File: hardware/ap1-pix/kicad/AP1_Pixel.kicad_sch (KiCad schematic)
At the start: 40 parts, among them J1 ENTRADA 5-24V, J2 PIXELES 1, J3 PIXELES 2, J4 PIXELES 3, J5 PIXELES 4, J7 PROGRAMADOR, U1 INA238, U2 LMR16006XDDC, U3 74HCT125D, U4 M24C02-WMN6TP

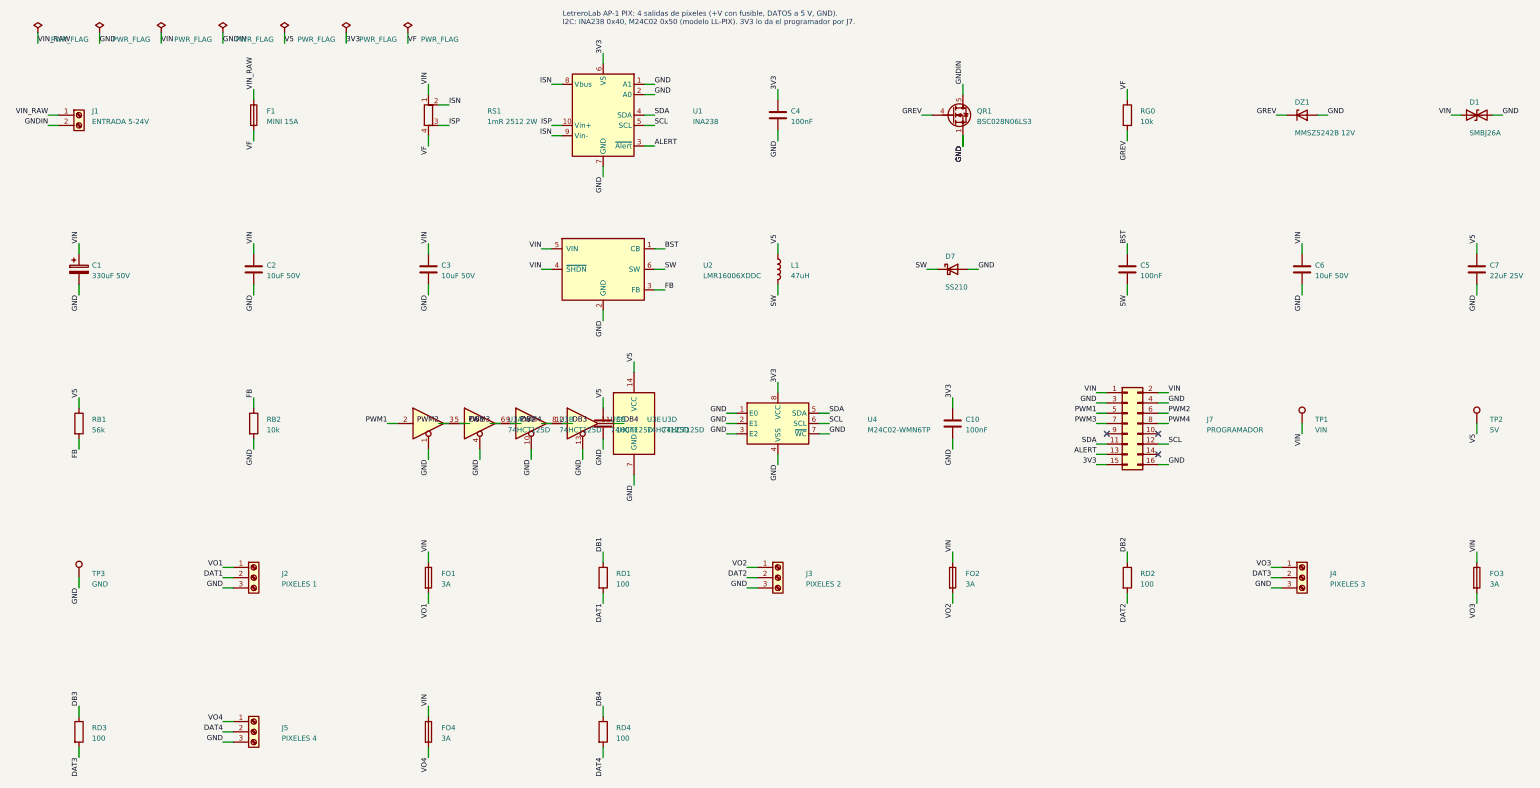
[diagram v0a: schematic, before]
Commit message: AP CONNECT: sin borneras en todas las placas, placa nueva AP PRO AI4 y guía de fabricantes
- Borneras de tornillo reemplazadas por conectores con cable y código LCSC verificado:
  XT60 (C98732), JST VH 2/3/4 (C160315/6/7), JST XH 2/3/4 (C158012, C144394/5), Qwiic
  en BASE, IND, PIX, DMX, PLANTILLA, AP INPUT, AP OUTPUT y DIST 4; zonas de potencia rehechas
- XT60 de la DIST 4 con la polaridad marcada en la huella (pata 1 = -, pata 2 = +)
- TCA9554PWR ya con código (C477924)
- ap1-ai4: 4 entradas 0-10 V / 4-20 mA con ADS1115 (C37593), +24 V para sensores de lazo
- Programa 1.7: lectura AI4, umbrales con acciones, Home Assistant, tarjeta en la app
- FABRICANTES.md: JLCPCB, PCBWay, Seeed, NextPCB, México; impresión 3D y tornillería
- Pedido JLCPCB con 10 placas (AP-0.2 retirada); ERC/DRC/DFM 0 en todas

Co-Authored-By: Claude Opus 5.5 <noreply@anthropic.com>
Claude-Session: https://claude.ai/code/session_01WVk3oGwfQfGTmAT2PMp8oW
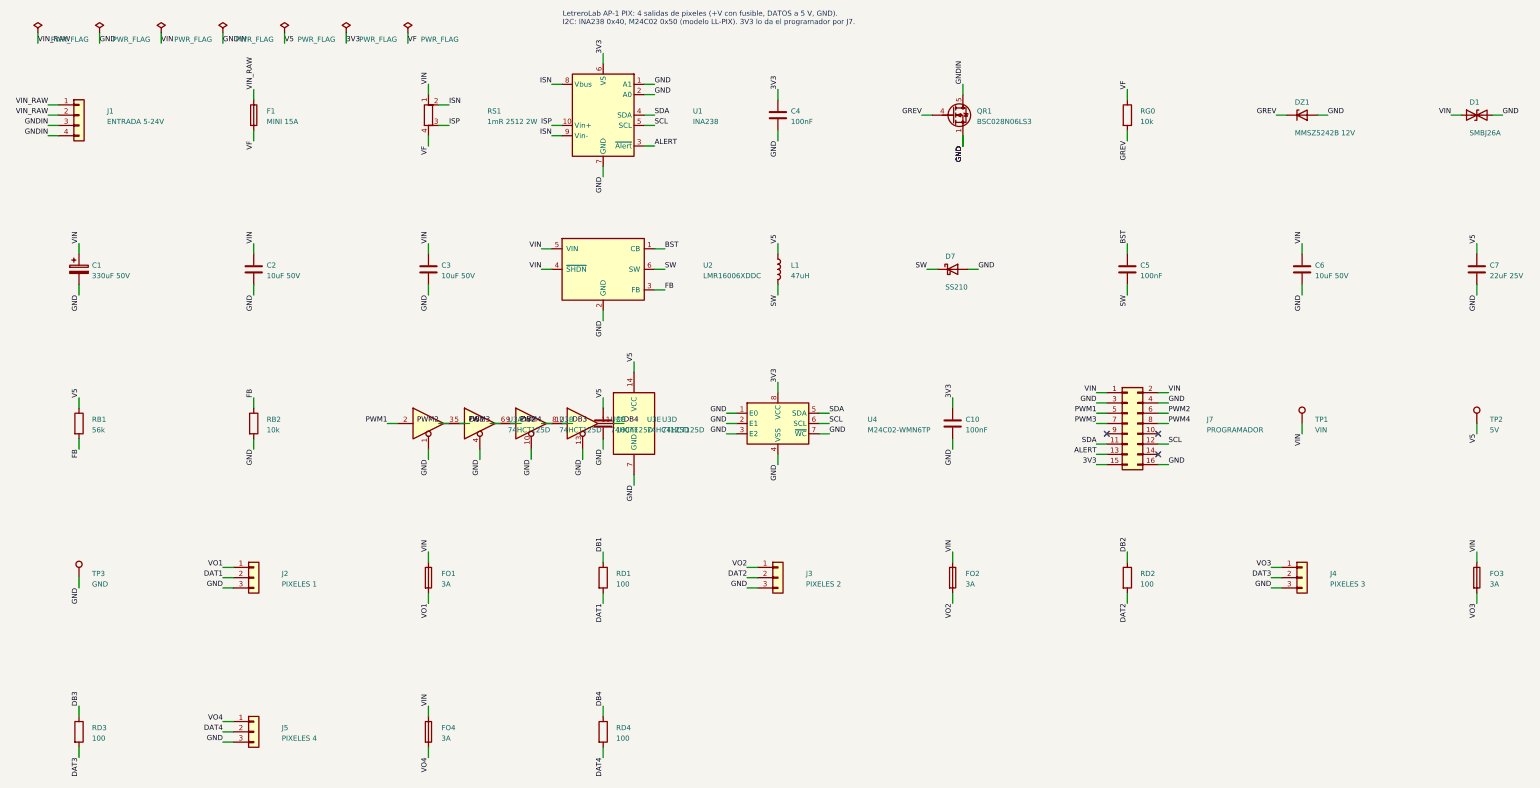
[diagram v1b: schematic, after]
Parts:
- J1: footprint TerminalBlock_Phoenix:TerminalBlock_Phoenix_MKDS-3-2-5.08_1x02_P5.08mm_Horizontal -> Connector_JST:JST_VH_B4P-VH_1x04_P3.96mm_Vertical; symbol Connector:Screw_Terminal_01x02 -> Connector_Generic:Conn_01x04
- J2, J3, J4, J5: footprint TerminalBlock_Phoenix:TerminalBlock_Phoenix_MKDS-3-3-5.08_1x03_P5.08mm_Horizontal -> Connector_JST:JST_VH_B3P-VH_1x03_P3.96mm_Vertical; symbol Connector:Screw_Terminal_01x03 -> Connector_Generic:Conn_01x03
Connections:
- net GNDIN: now also J1.3 (Pin_3), J1.4 (Pin_4); no longer J1.2 (Pin_2)
- net VIN_RAW: now also J1.2 (Pin_2)
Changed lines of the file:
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@@
 	(title_block
 		(title "LetreroLab AP-1 PIX - módulo de pixeles direccionables")
-		(date "2026-10-05")
+		(date "2026-10-06")
 		(rev "1.0")
 		(company "PCB 88 x 56 mm, 2 capas, cobre 2 oz")
@@
 	)
 	(symbol
-		(lib_id "Connector:Screw_Terminal_01x02")
+		(lib_id "Connector_Generic:Conn_01x04")
 		(at 30.48 40.64 0)
 		(unit 1)
@@
 		(dnp no)
 		(property "Reference" "J1"
-			(at 33.68 39.64 0)
+			(at 37.4 39.64 0)
 			(effects
 				(font
@@
 		)
 		(property "Value" "ENTRADA 5-24V"
-			(at 33.68 42.24 0)
+			(at 37.4 42.24 0)
 			(effects
 				(font
@@
 			)
 		)
-		(property "Footprint" "TerminalBlock_Phoenix:TerminalBlock_Phoenix_MKDS-3-2-5.08_1x02_P5.08mm_Horizontal"
+		(property "Footprint" "Connector_JST:JST_VH_B4P-VH_1x04_P3.96mm_Vertical"
 			(at 30.48 40.64 0)
 			(hide yes)
@@
 		(pin "2"
 		)
+		(pin "3"
+		)
+		(pin "4"
+		)
 		(instances
 			(project "AP1_Pixel"
@@
 	(wire
 		(pts
+			(xy 25.4 38.1)
+			(xy 22.86 38.1)
+		)
+		(stroke
+			(width 0)
+			(type default)
+		)
+	)
+	(label "VIN_RAW"
+		(at 22.86 38.1 180)
+		(fields_autoplaced yes)
+		(effects
+			(font
+				(size 1.27 1.27)
+			)
+			(justify right bottom)
+		)
+	)
+	(wire
+		(pts
 			(xy 25.4 40.64)
 			(xy 22.86 40.64)
@@
 		)
 	)
+	(wire
+		(pts
+			(xy 25.4 45.72)
+			(xy 22.86 45.72)
+		)
+		(stroke
+			(width 0)
+			(type default)
+		)
+	)
+	(label "GNDIN"
+		(at 22.86 45.72 180)
+		(fields_autoplaced yes)
+		(effects
+			(font
+				(size 1.27 1.27)
+			)
+			(justify right bottom)
+		)
+	)
 	(symbol
 		(lib_id "Device:Fuse")
@@
 	)
 	(symbol
-		(lib_id "Connector:Screw_Terminal_01x03")
+		(lib_id "Connector_Generic:Conn_01x03")
 		(at 73.66 154.94 0)
 		(unit 1)
@@
 			)
 		)
-		(property "Footprint" "TerminalBlock_Phoenix:TerminalBlock_Phoenix_MKDS-3-3-5.08_1x03_P5.08mm_Horizontal"
+		(property "Footprint" "Connector_JST:JST_VH_B3P-VH_1x03_P3.96mm_Vertical"
 			(at 73.66 154.94 0)
 			(hide yes)
@@
 	)
 	(symbol
-		(lib_id "Connector:Screw_Terminal_01x03")
+		(lib_id "Connector_Generic:Conn_01x03")
 		(at 203.2 154.94 0)
 		(unit 1)
@@
 			)
 		)
-		(property "Footprint" "TerminalBlock_Phoenix:TerminalBlock_Phoenix_MKDS-3-3-5.08_1x03_P5.08mm_Horizontal"
+		(property "Footprint" "Connector_JST:JST_VH_B3P-VH_1x03_P3.96mm_Vertical"
 			(at 203.2 154.94 0)
 			(hide yes)
@@
 	)
 	(symbol
-		(lib_id "Connector:Screw_Terminal_01x03")
+		(lib_id "Connector_Generic:Conn_01x03")
 		(at 332.74 154.94 0)
 		(unit 1)
@@
 			)
 		)
-		(property "Footprint" "TerminalBlock_Phoenix:TerminalBlock_Phoenix_MKDS-3-3-5.08_1x03_P5.08mm_Horizontal"
+		(property "Footprint" "Connector_JST:JST_VH_B3P-VH_1x03_P3.96mm_Vertical"
 			(at 332.74 154.94 0)
 			(hide yes)
@@
 	)
 	(symbol
-		(lib_id "Connector:Screw_Terminal_01x03")
+		(lib_id "Connector_Generic:Conn_01x03")
 		(at 73.66 193.04 0)
 		(unit 1)
@@
 			)
 		)
-		(property "Footprint" "TerminalBlock_Phoenix:TerminalBlock_Phoenix_MKDS-3-3-5.08_1x03_P5.08mm_Horizontal"
+		(property "Footprint" "Connector_JST:JST_VH_B3P-VH_1x03_P3.96mm_Vertical"
 			(at 73.66 193.04 0)
 			(hide yes)
